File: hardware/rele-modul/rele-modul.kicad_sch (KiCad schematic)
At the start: 0 parts

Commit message: Hardver: relémodul kapcsolási rajz (vázlat) + modulmag hierarchikus lapként
ULN2803A + 4 × Schrack RTD14024, kimenet COM + NO (D62), csatornánként
visszajelző LED, HW-ID 10k/10k (4. sáv). A modulmag kiadja a +24V_P-t is
(relétáp), és mindhárom modulprojekthez tartalmazza a hivatkozásokat.
ERC: 0 hiba (4 lib_symbol_mismatch figyelmeztetés a relé-szimbólumon).

Co-Authored-By: Claude Opus 5.5 <noreply@anthropic.com>
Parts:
- added C101: 100n, Capacitor_SMD:C_0603_1608Metric, symbol Device:C
- added D101, D102, D103, D104: zöld, LED_SMD:LED_0603_1608Metric, symbol Device:LED
- added J100: 24V IN, TerminalBlock_Phoenix:TerminalBlock_Phoenix_PT-1,5-2-5.0-H_1x02_P5.00mm_Horizontal, symbol Connector_Generic:Conn_01x02
- added J101: RELÉ 1, TerminalBlock_Phoenix:TerminalBlock_Phoenix_MKDS-3-2-5.08_1x02_P5.08mm_Horizontal, symbol Connector_Generic:Conn_01x02
- added J102: RELÉ 2, TerminalBlock_Phoenix:TerminalBlock_Phoenix_MKDS-3-2-5.08_1x02_P5.08mm_Horizontal, symbol Connector_Generic:Conn_01x02
- added J103: RELÉ 3, TerminalBlock_Phoenix:TerminalBlock_Phoenix_MKDS-3-2-5.08_1x02_P5.08mm_Horizontal, symbol Connector_Generic:Conn_01x02
- added J104: RELÉ 4, TerminalBlock_Phoenix:TerminalBlock_Phoenix_MKDS-3-2-5.08_1x02_P5.08mm_Horizontal, symbol Connector_Generic:Conn_01x02
- added K1, K2, K3, K4: RTD14024, Relay_THT:Relay_SPDT_Schrack-RT1-16A-FormC_RM5mm, symbol Relay:Relay_SPDT
- added R101, R102: 10k 1%, Resistor_SMD:R_0603_1608Metric, symbol Device:R
- added R103, R104, R105, R106: 10k, Resistor_SMD:R_0805_2012Metric, symbol Device:R
- added U101: ULN2803ADWR, Package_SO:SOIC-18W_7.5x11.6mm_P1.27mm, symbol Transistor_Array:ULN2803A
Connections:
- new net +24V_IN: J100.1 (Pin_1)
- new net +24V_P: K1.A1, K2.A1, K3.A1, K4.A1, R103.1, R104.1, R105.1, R106.1, U101.10 (COM)
- new net +3V3: R101.1
- new net COIL1: D101.1 (K), K1.A2, U101.18 (O1)
- new net COIL2: D102.1 (K), K2.A2, U101.17 (O2)
- new net COIL3: D103.1 (K), K3.A2, U101.16 (O3)
- new net COIL4: D104.1 (K), K4.A2, U101.15 (O4)
- new net GND: C101.2, J100.2 (Pin_2), R102.2, U101.5 (I5), U101.6 (I6), U101.7 (I7), U101.8 (I8), U101.9 (GND)
- new net HW_ID: C101.1, R101.2, R102.1
- new net LED1_A: D101.2 (A), R103.2
- new net LED2_A: D102.2 (A), R104.2
- new net LED3_A: D103.2 (A), R105.2
- new net LED4_A: D104.2 (A), R106.2
- new net OUT1_COM: J101.1 (Pin_1), K1.11
- new net OUT1_NO: J101.2 (Pin_2), K1.14
- new net OUT2_COM: J102.1 (Pin_1), K2.11
- new net OUT2_NO: J102.2 (Pin_2), K2.14
- new net OUT3_COM: J103.1 (Pin_1), K3.11
- new net OUT3_NO: J103.2 (Pin_2), K3.14
- new net OUT4_COM: J104.1 (Pin_1), K4.11
- new net OUT4_NO: J104.2 (Pin_2), K4.14
- new net REL1: U101.1 (I1)
- new net REL2: U101.2 (I2)
- new net REL3: U101.3 (I3)
- new net REL4: U101.4 (I4)
- no-connect marks 0 -> 28
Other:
- added sheet modulmag (../modulmag/modulmag.kicad_sch)
- note added: "230 V: ≥ 8 mm kúszóút + légköz a törpefeszültségű résztől, marás a relék alatt; a hálózati rész alatt egyik rétegen sincs törpefeszültségű réz (D62)"
- note added: "HW-ID: relé = 4. sáv (1,65 V)"
- note added: "MODULMAG (../modulmag/modulmag.kicad_sch): táp, STM32F303RET6, ISO1042, busz-csatlakozók (J2/J3), lezárás"
- note added: "RELÉK – Schrack RTD14024 (1 váltó, 16 A / 250 V AC, 24 V DC, 400 mW): kimenet csak COM + NO, az NC (12) nincs kivezetve"
- note added: "RELÉMEGHAJTÓ – ULN2803A: a belső kioltó diódák a COM-on (10) át a +24V_P-re; a bemenetek belső lehúzása → bekapcsoláskor minden relé KI"
- note added: "Visszajelző LED: +24V_P – 10 k – LED – a relé tekercsének alsó vége (ULN-kimenet) → ~2 mA, ha a relé BE"
- note added: "VÁZLAT – generálva a MODULMAG-SPEC + D62 alapján (2026-10-14). Elrendezést rendezd; a bekötés címkékkel kész."
- title: Relémodul (4 relé) -> Relémodul – 4 × RTD14024 (16 A, 230 V), modulmag

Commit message: Hardver: mind az öt kapcsolási rajz elrendezve (vezetékes, blokkos), netlista-ellenőrzővel
Funkcionális blokkok, balról jobbra jelút, tápsín felül / GND alul; blokkon belül
vezeték, blokkok között és az IC-lábakon címke. kigen: lábpozíció, place(),
wire/junction/rail, tükrözés, 1,27 mm-es rács, olvasható mezők. gen/netcmp.py:
két netlista lábszintű összevetése – a bekötés az átrendezés előttivel azonos
(a modulmag D66-os D6/JP2-jét kivéve). ERC: 0 hiba mind az öt lapon.

Co-Authored-By: Claude Opus 5.5 <noreply@anthropic.com>
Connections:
- net LED1_A: no longer names the net of D101.2 (A), R103.2
- net LED2_A: no longer names the net of D102.2 (A), R104.2
- net LED3_A: no longer names the net of D103.2 (A), R105.2
- net LED4_A: no longer names the net of D104.2 (A), R106.2
- net OUT1_COM: no longer names the net of J101.1 (Pin_1), K1.11
- net OUT1_NO: no longer names the net of J101.2 (Pin_2), K1.14
- net OUT2_COM: no longer names the net of J102.1 (Pin_1), K2.11
- net OUT2_NO: no longer names the net of J102.2 (Pin_2), K2.14
- net OUT3_COM: no longer names the net of J103.1 (Pin_1), K3.11
- net OUT3_NO: no longer names the net of J103.2 (Pin_2), K3.14
- net OUT4_COM: no longer names the net of J104.1 (Pin_1), K4.11
- net OUT4_NO: no longer names the net of J104.2 (Pin_2), K4.14
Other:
- note added: "24 V betáp (J100)"
- note added: "Generálva (hardware/gen/rele-modul.py) – a MODULMAG-SPEC + D62 alapján; kézi szerkesztés helyett a generátort módosítsd."
- note added: "RELÉMEGHAJTÓ – ULN2803A: belső kioltó diódák"
- note added: "Visszajelző LED: +24V_P – 10 k – LED – a tekercs alsó vége (ULN-kimenet) → ~2 mA, ha a relé BE"
- note added: "a COM-on (10) át a +24V_P-re; a bemenetek belső"
- note added: "lehúzása → bekapcsoláskor minden relé KI"
- note removed: "RELÉMEGHAJTÓ – ULN2803A: a belső kioltó diódák a COM-on (10) át a +24V_P-re; a bemenetek belső lehúzása → bekapcsoláskor minden relé KI"
- note removed: "Visszajelző LED: +24V_P – 10 k – LED – a relé tekercsének alsó vége (ULN-kimenet) → ~2 mA, ha a relé BE"
- note removed: "VÁZLAT – generálva a MODULMAG-SPEC + D62 alapján (2026-10-14). Elrendezést rendezd; a bekötés címkékkel kész."

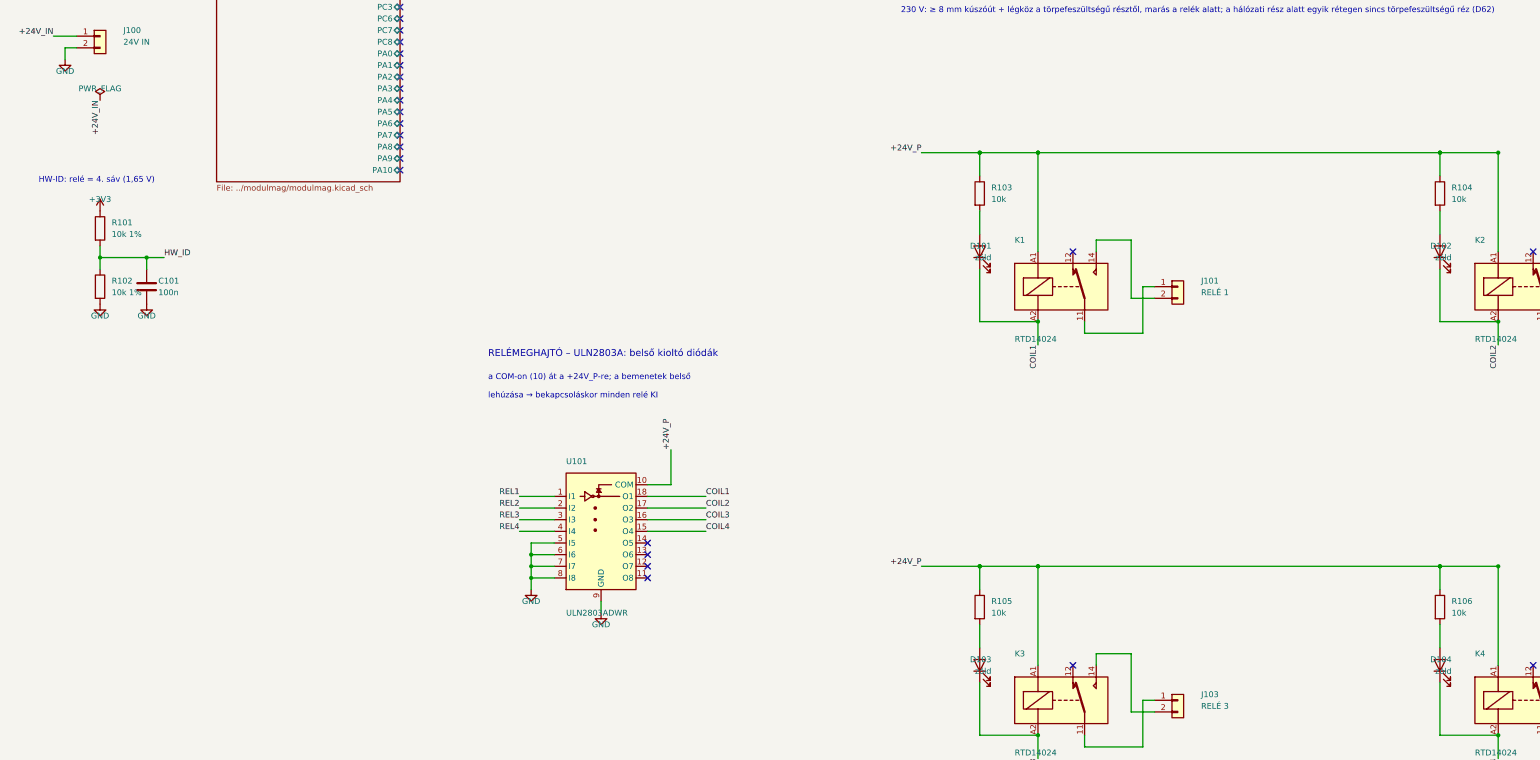
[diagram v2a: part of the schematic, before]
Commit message: Hardver: kapcsolási rajzok olvashatósága (KiCad MCP vizuális ellenőrzés alapján), output/ gitignore
Co-Authored-By: Claude Opus 5.5 <noreply@anthropic.com>
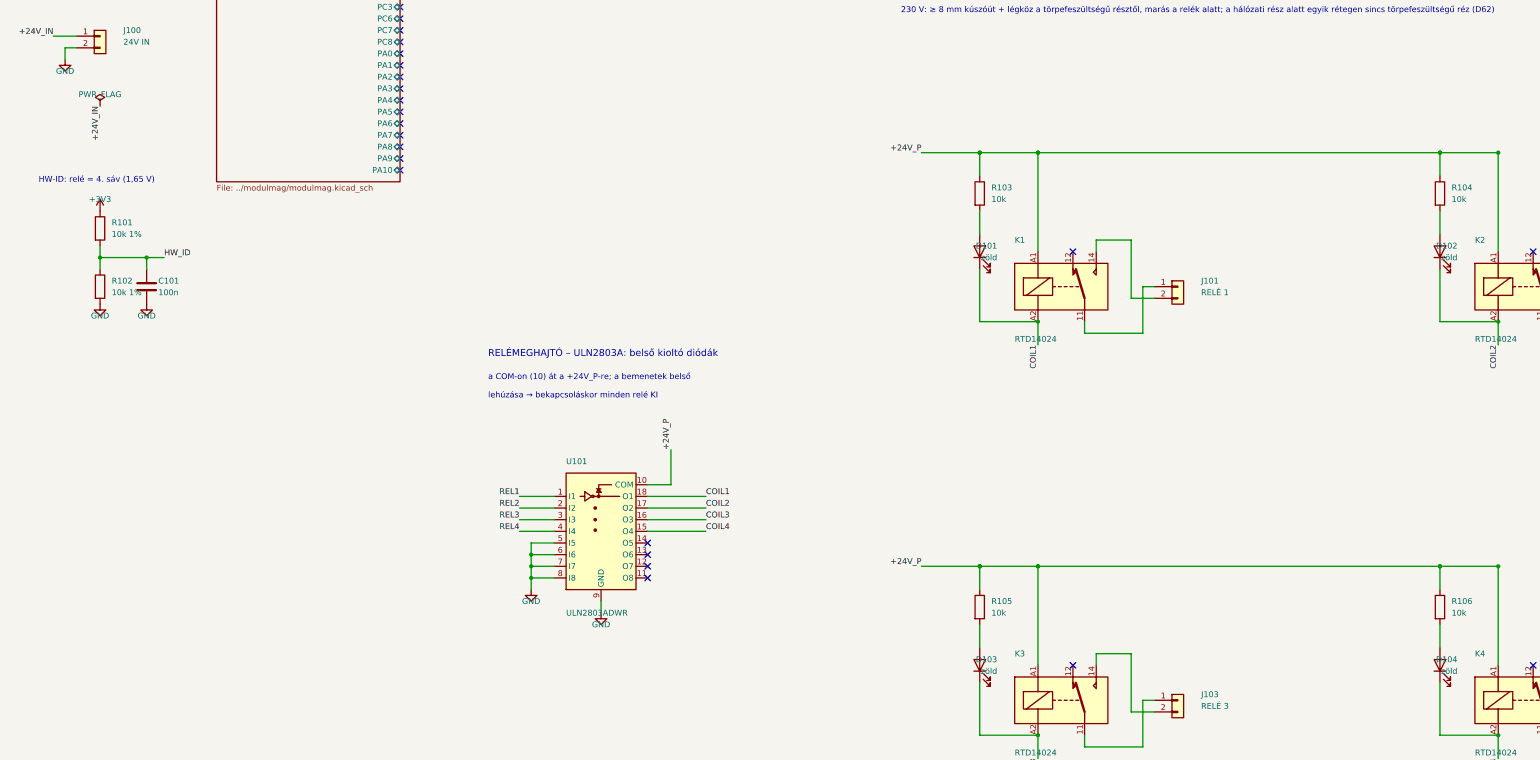
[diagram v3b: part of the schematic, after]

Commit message: Hardver: átnézés (C320 javítva), LoRa-előkészítés (D68), bővítők (D69), R6/R7 = 0 Ω (D70)
- bemeneti modul: a HDC3020 hidegítője C330 lett (a C320 kétszer szerepelt);
  a generátor mostantól hibát dob duplikált jelölésre
- vezérlő: E22-900M22S LoRa + u.FL + 74LVC1G04, minden DNP; J8 bővítő (GPIO5),
  7 mérőpont; spec szerinti DNP-k (USB C, 1 MΩ, PMODE, CAN-fojtó + áthidalók);
  saját footprint az LMR36015-höz (RNX) és az E22-höz
- modulmag: HW_REV osztó (PB0), DNP J4 2 × 5 bővítő; relé: DNP SCT-013 → PA0
- mind az öt lap vizuálisan rendbe téve; R6/R7 = 0 Ω
- specek és döntésnapló frissítve (D68–D70)

Co-Authored-By: Claude Opus 5.5 <noreply@anthropic.com>
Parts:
- added C102: 10µ, Capacitor_SMD:C_0805_2012Metric, symbol Device:C
- added C103: 10n, Capacitor_SMD:C_0603_1608Metric, symbol Device:C
- added J105: SCT-013, Connector_Audio:Jack_3.5mm_CUI_SJ1-3523N_Horizontal, symbol Connector_Audio:AudioJack3
- added R107, R108: 10k, Resistor_SMD:R_0603_1608Metric, symbol Device:R
- added R109: DNP, Resistor_SMD:R_0603_1608Metric, symbol Device:R
- added R110: 1k, Resistor_SMD:R_0603_1608Metric, symbol Device:R
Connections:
- net +3V3: now also R107.1
- net GND: now also C102.2, C103.2, R108.2
- new net: C102.1, J105.S, R107.2, R108.1, R109.1
- new net: J105.T, R109.2, R110.1
- new net CT_SENSE: C103.1, R110.2
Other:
- note added: "FOGYASZTÁSMÉRÉS (D37, D69) – minden DNP: SCT-013 lakatfogós áramváltó 3,5 mm-es jackre → PA0 (ADC)"
- note added: "SCT-013-030 (1 V kimenet): R109 nincs; áramkimenetes típushoz R109 = terhelő-ellenállás"

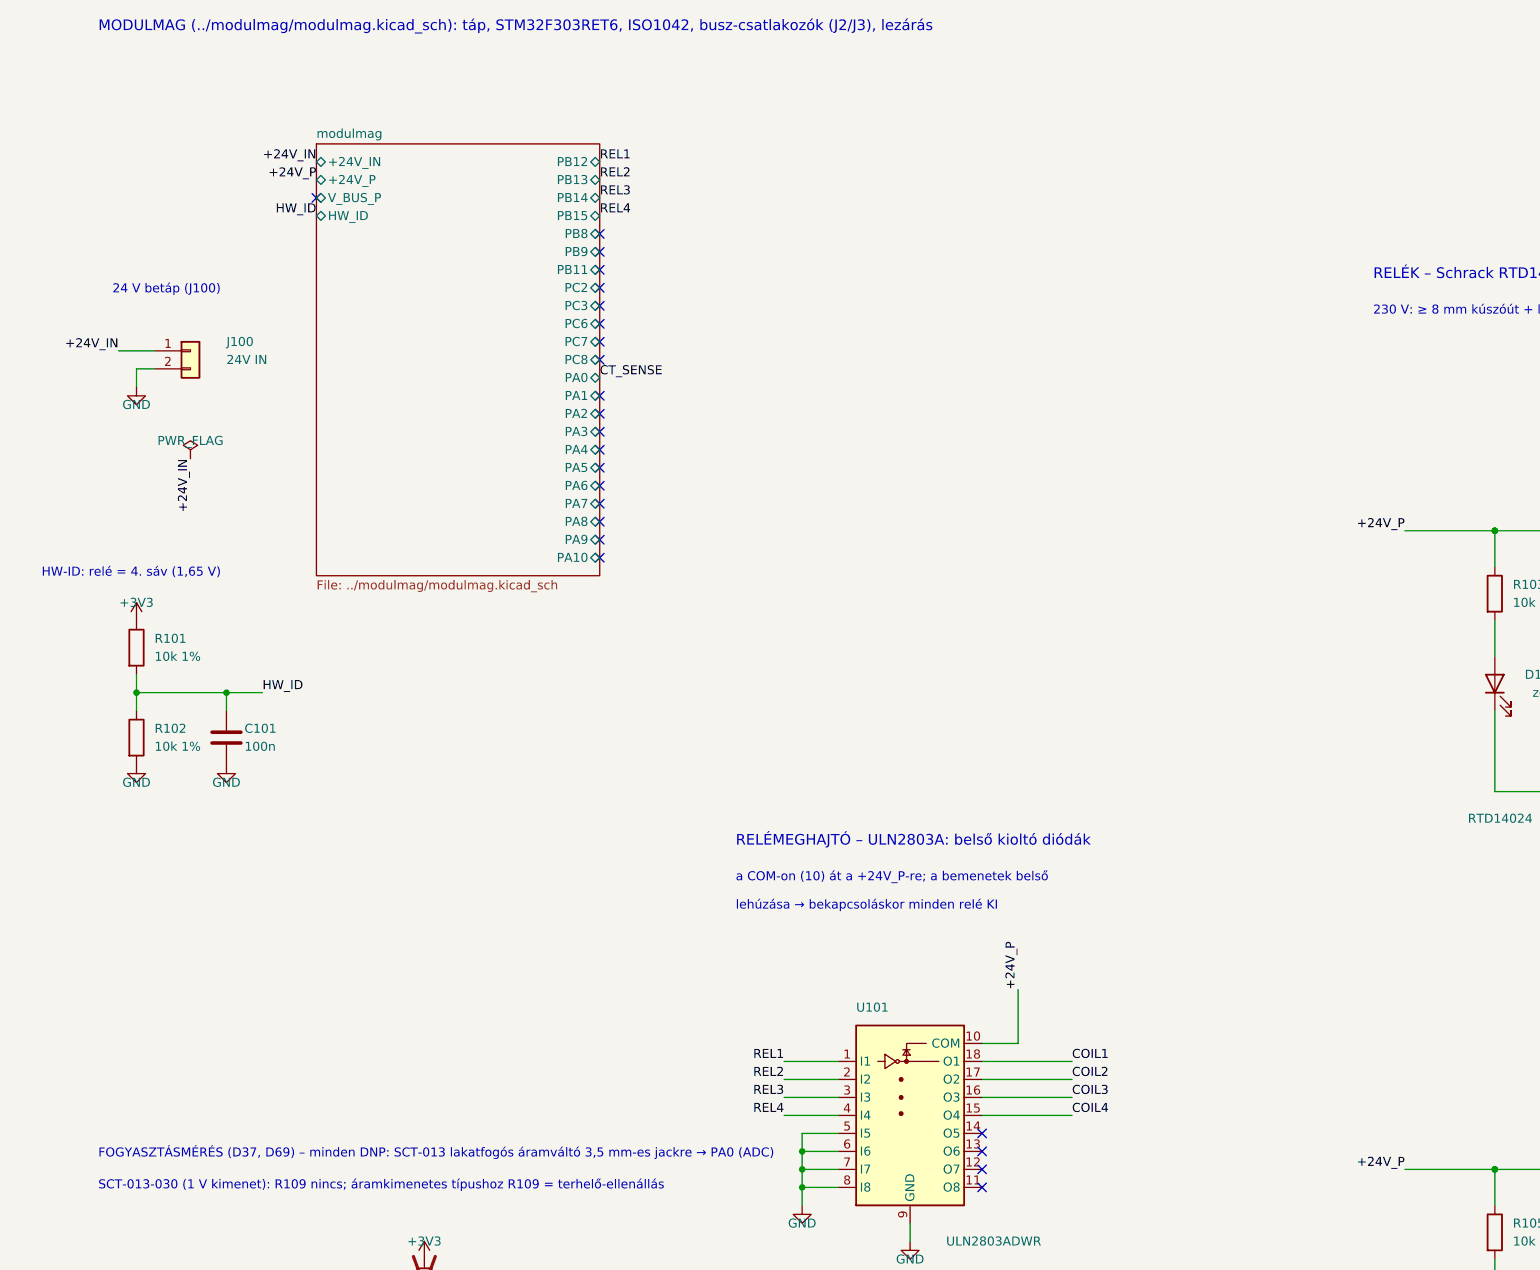
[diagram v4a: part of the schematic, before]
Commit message: Hardver: központi 5 V, közös föld, 12–26 V, HW-ID 16 sáv (D71)
Vezérlő: LMR33630 (5,2 V) + LM66200 (USB-vel VAGY-olva) + TPS259531 eFuse (2 A);
F1 2 A, D1 B360 a 12 V-os működéshez. Modulmag: táp a buszról (AP2112K), TCAN1044AV,
nincs izoláció, PC1 = VBUS_SENSE. LED/relé: VIN_SENSE a PB11-en, relémodul saját
tekercs-táppal. Bemeneti modul: nincs 24 V. HW-ID/HW_REV 16 sáv. Specifikációk,
áttekintés, beszerzés, ütemterv frissítve.

Co-Authored-By: Claude Opus 5.5 <noreply@anthropic.com>
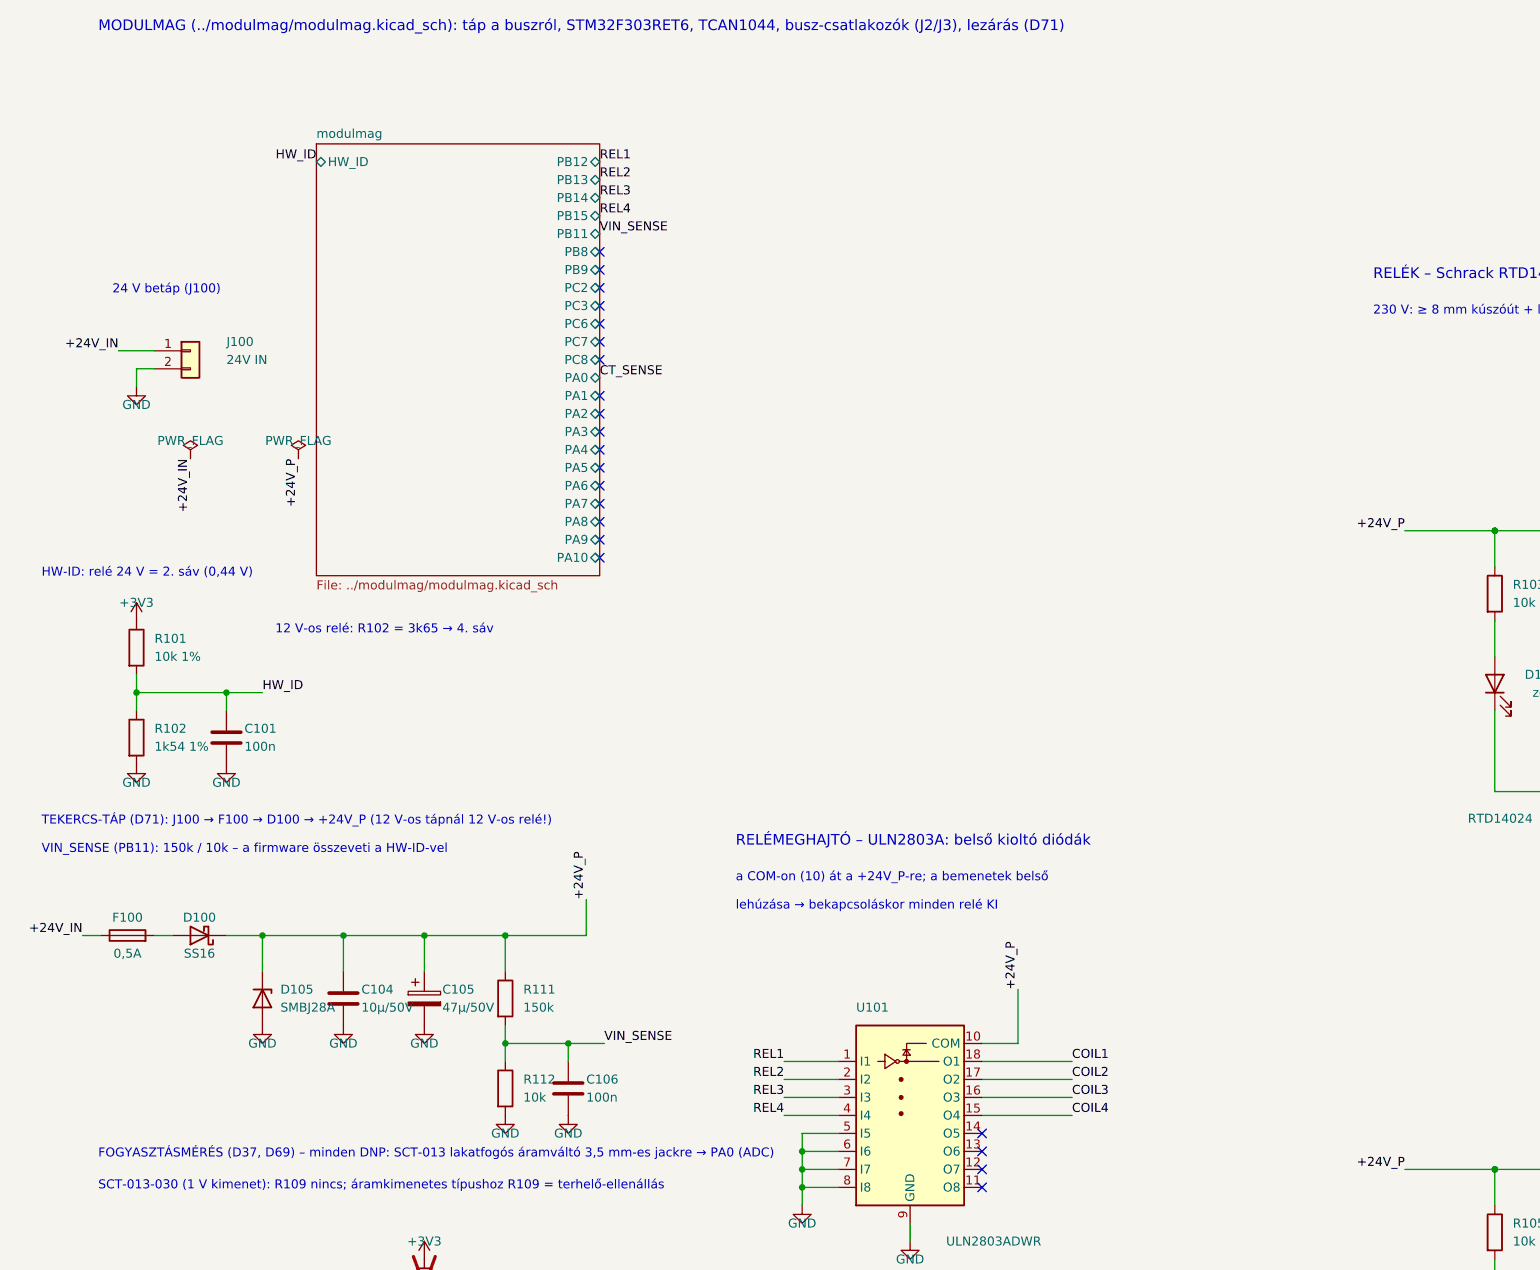
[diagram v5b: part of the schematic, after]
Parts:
- added C104: 10µ/50V, Capacitor_SMD:C_1210_3225Metric, symbol Device:C
- added C105: 47µ/50V, Capacitor_SMD:CP_Elec_6.3x7.7, symbol Device:C_Polarized
- added C106: 100n, Capacitor_SMD:C_0603_1608Metric, symbol Device:C
- added D100: SS16, Diode_SMD:D_SMA, symbol Device:D_Schottky
- added D105: SMBJ28A, Diode_SMD:D_SMB, symbol Device:D_Zener
- added F100: 0,5A, Fuse:Fuse_1206_3216Metric, symbol Device:Fuse
- added R111: 150k, Resistor_SMD:R_0603_1608Metric, symbol Device:R
- added R112: 10k, Resistor_SMD:R_0603_1608Metric, symbol Device:R
- R102: value 10k 1% -> 1k54 1%; Megjegyzés (none) -> 24 V-os tekercs: 1,54k (2. sáv); 12 V-os tekercs: 3,65k (4.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
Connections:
- net +24V_IN: now also F100.1
- net +24V_P: now also C104.1, C105.1, D100.1 (K), D105.1 (K), R111.1
- net GND: now also C104.2, C105.2, C106.2, D105.2 (A), R112.2
- new net: D100.2 (A), F100.2
- new net VIN_SENSE: C106.1, R111.2, R112.1
- no-connect marks 28 -> 26
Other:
- sheet modulmag ports: added none; removed +24V_IN, +24V_P, V_BUS_P
- note added: "12 V-os relé: R102 = 3k65 → 4. sáv"
- note added: "HW-ID: relé 24 V = 2. sáv (0,44 V)"
- note added: "MODULMAG (../modulmag/modulmag.kicad_sch): táp a buszról, STM32F303RET6, TCAN1044, busz-csatlakozók (J2/J3), lezárás (D71)"
- note added: "TEKERCS-TÁP (D71): J100 → F100 → D100 → +24V_P (12 V-os tápnál 12 V-os relé!)"
- note added: "VIN_SENSE (PB11): 150k / 10k – a firmware összeveti a HW-ID-vel"
- note removed: "HW-ID: relé = 4. sáv (1,65 V)"
- note removed: "MODULMAG (../modulmag/modulmag.kicad_sch): táp, STM32F303RET6, ISO1042, busz-csatlakozók (J2/J3), lezárás"
